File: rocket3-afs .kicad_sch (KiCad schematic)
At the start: 85 parts, among them J1 ARMING_PLUG, J2 POWER, J3 E-MATCH_DROGUE, J4 SWD, J5 E-MATCH_RECOVERY, Q1 Q_NMOS_GSD, Q2 Q_NMOS_GSD, Q3 Q_NMOS_GSD, Q4 Q_NMOS_GSD, Q5 Q_NMOS_GSD, U7 MP1584EN-LF-Z, U8 USBLC6-2SC6, U9 MMC5983MA, Y1 16MHz

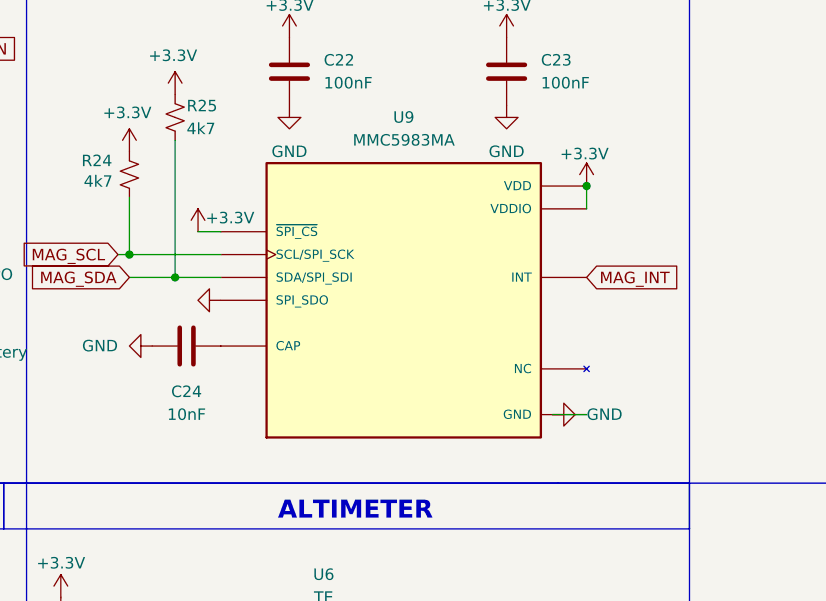
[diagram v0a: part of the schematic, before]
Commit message: Typo change on cap for magnetometer
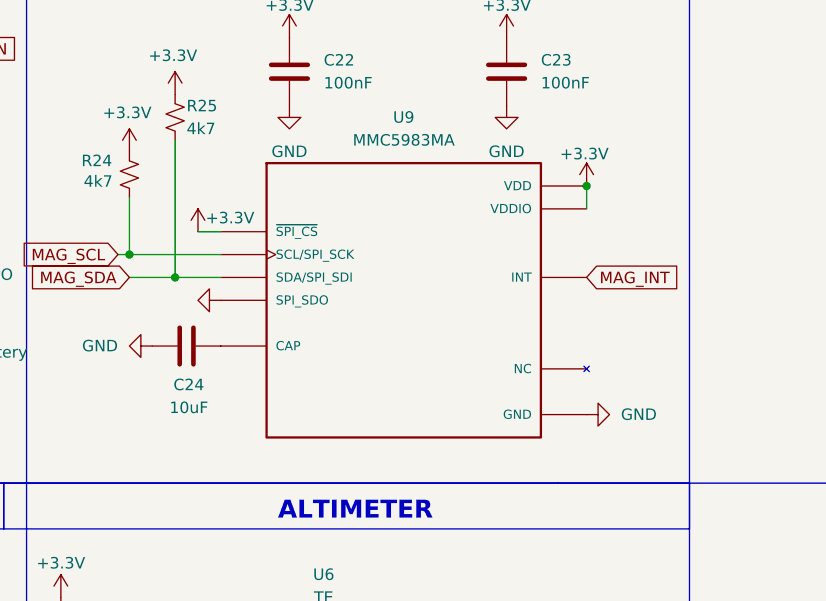
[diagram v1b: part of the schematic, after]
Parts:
- C24: value 10nF -> 10uF
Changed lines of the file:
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@@
 	(wire
 		(pts
-			(xy 287.02 123.19) (xy 283.21 123.19)
-		)
-		(stroke
-			(width 0)
-			(type default)
-		)
-	)
-	(wire
-		(pts
 			(xy 214.63 180.34) (xy 219.71 180.34)
 		)
@@
 		(on_board yes)
 		(dnp no)
-		(fields_autoplaced yes)
 		(property "Reference" "C24"
-			(at 242.57 120.65 90)
+			(at 242.824 119.888 90)
 			(effects
 				(font
@@
 			)
 		)
-		(property "Value" "10nF"
-			(at 242.57 123.19 90)
+		(property "Value" "10uF"
+			(at 242.824 122.428 90)
 			(effects
 				(font
@@
 		(lib_name "GND_3")
 		(lib_id "power:GND")
-		(at 283.21 123.19 90)
+		(at 287.02 123.19 90)
 		(unit 1)
 		(exclude_from_sim no)
@@
 		(fields_autoplaced yes)
 		(property "Reference" "#PWR095"
-			(at 289.56 123.19 0)
+			(at 293.37 123.19 0)
 			(effects
 				(font
@@
 		)
 		(property "Value" "GND"
-			(at 287.02 123.1899 90)
+			(at 290.83 123.1899 90)
 			(effects
 				(font
@@
 		)
 		(property "Footprint" ""
-			(at 283.21 123.19 0)
+			(at 287.02 123.19 0)
 			(effects
 				(font
@@
 		)
 		(property "Datasheet" ""
-			(at 283.21 123.19 0)
+			(at 287.02 123.19 0)
 			(effects
 				(font
@@
 		)
 		(property "Description" "Power symbol creates a global label with name \"GND\" , ground"
-			(at 283.21 123.19 0)
+			(at 287.02 123.19 0)
 			(effects
 				(font

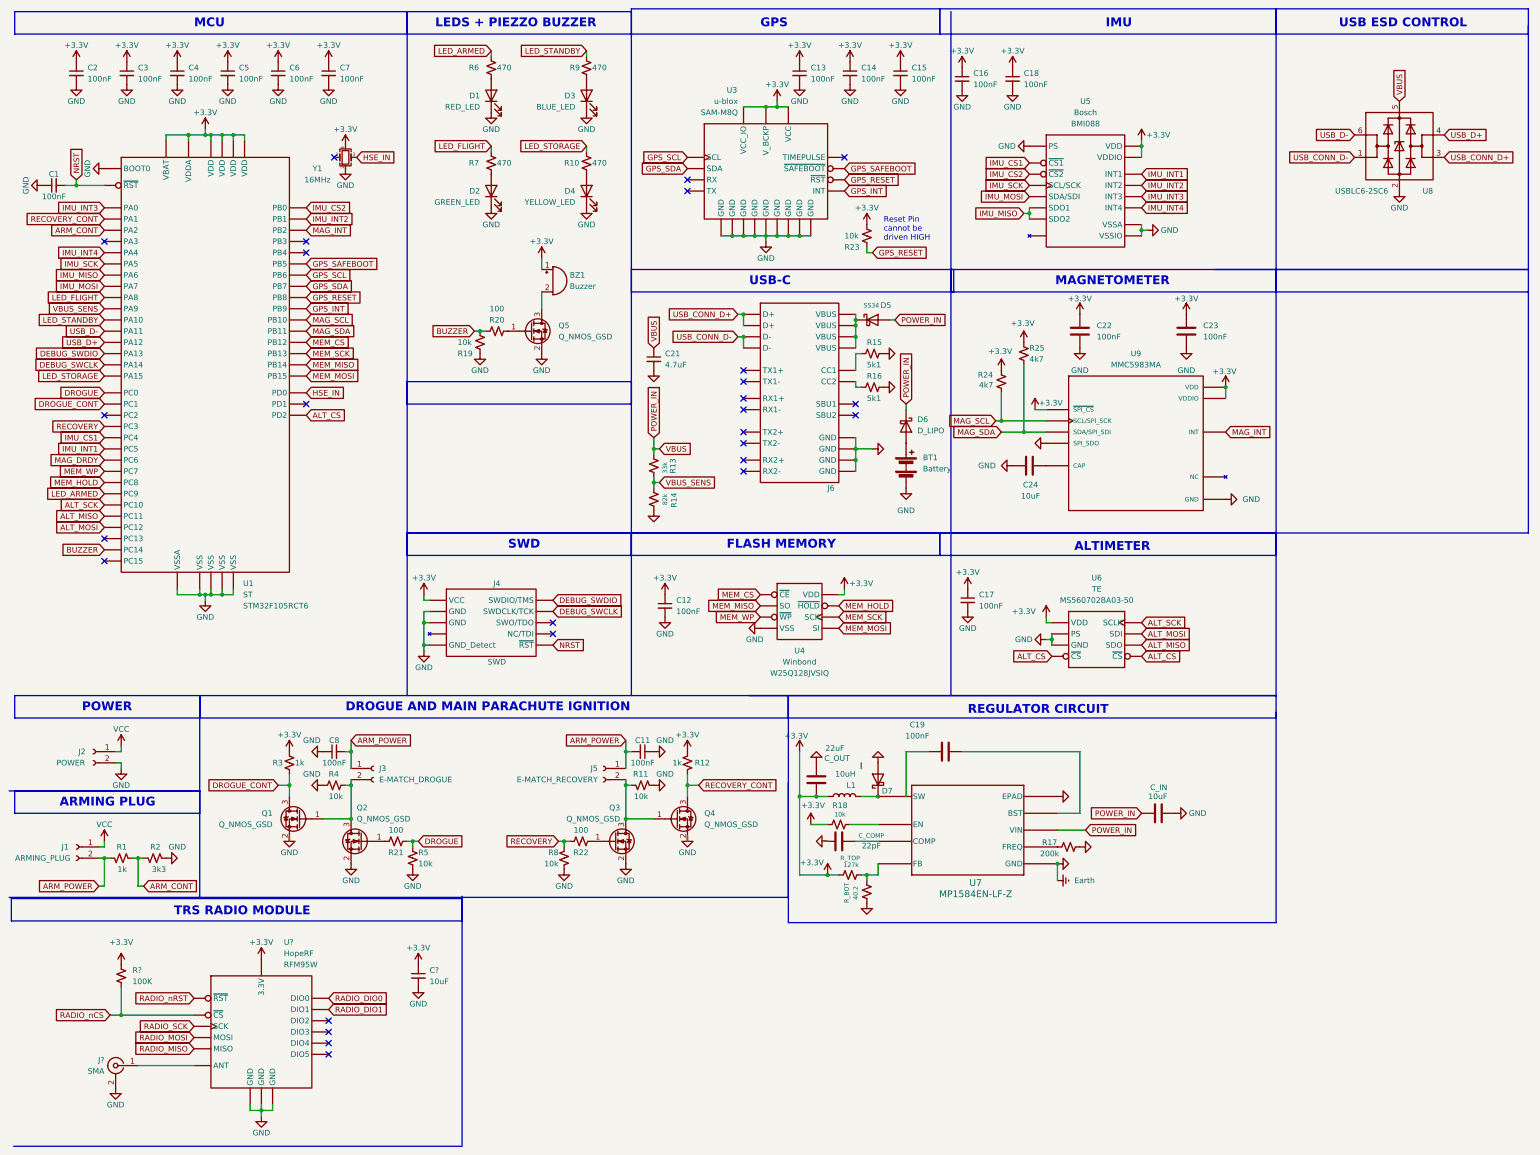
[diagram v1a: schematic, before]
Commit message: regulator circuit cleanup, added servo power and control circuits
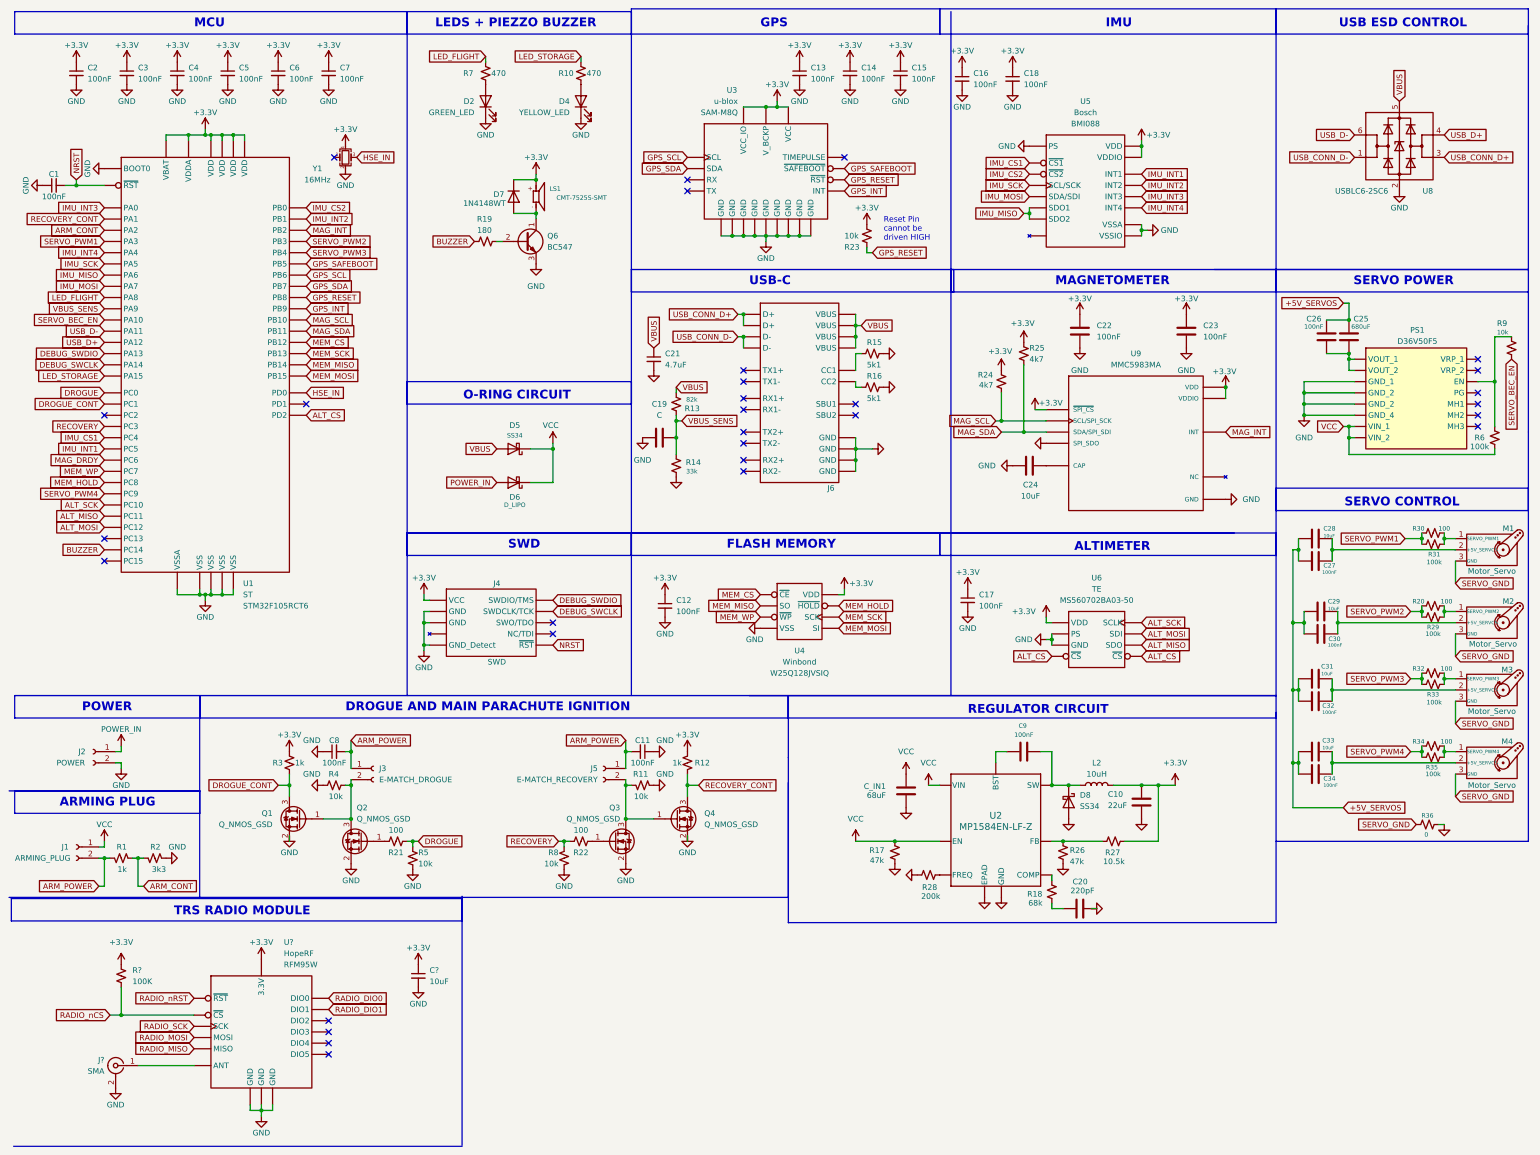
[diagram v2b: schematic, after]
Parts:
- removed BT1: Battery, symbol Device:Battery
- removed BZ1: Buzzer, Buzzer_Beeper:Buzzer_CUI_CPT-9019S-SMT, symbol Device:Buzzer
- removed C_COMP: 22pF, symbol Device:C
- removed C_IN: 10uF, symbol Device:C
- removed C_OUT: 22uF, symbol Device:C
- removed D1: RED_LED, Diode_SMD:D_0603_1608Metric, symbol Device:LED
- removed D3: BLUE_LED, Diode_SMD:D_0603_1608Metric, symbol Device:LED
- removed D7: SS34, Diode_SMD:D_SMA, symbol Diode:SS34
- removed L1: 10uH, symbol Device:L
- removed Q5: Q_NMOS_GSD, Package_TO_SOT_SMD:TSOT-23, symbol Device:Q_NMOS_GSD
- removed R_BOT: 40.2, symbol Device:R_Small_US
- removed R_TOP: 127k, symbol Device:R_Small_US
- removed U7: MP1584EN-LF-Z, SOIC8E_MPS, symbol 2025-08-17_10-37-18:MP1584EN-LF-Z
- added C10: 22uF, symbol Device:C
- added C20: 220pF, symbol Device:C
- added C25: 680uF, symbol Device:C
- added C26, C27, C30, C32, C34, C9: 100nF, symbol Device:C
- added C28, C29, C31, C33: 10uF, symbol Device:C
- added C_IN1: 68uF, symbol Device:C
- added D7: 1N4148WT, Diode_SMD:D_SOD-523, symbol Diode:1N4148WT
- added D8: SS34, Diode_SMD:D_SMA, symbol Diode:SS34
- added L2: 10uH, symbol Device:L
- added LS1: CMT-7525S-SMT, CMT-7525S-SMT:CUI_CMT-7525S-SMT, symbol CMT-7525S-SMT:CMT-7525S-SMT
- added M1, M2, M3, M4: Motor_Servo, symbol Motor:Motor_Servo
- added PS1: D36V50F5, D36V50F5, symbol D36V50F5:D36V50F5
- added Q6: BC547, Package_TO_SOT_THT:TO-92_Inline, symbol Transistor_BJT:BC547
- added R26: 47k, symbol Device:R_Small_US
- added R27: 10.5k, symbol Device:R_Small_US
- added R28: 200k, symbol Device:R_Small_US
- added R29, R31, R33, R35: 100k, symbol Device:R_Small_US
- added R30, R32, R34: 100, symbol Device:R_Small_US
- added R36: 0, symbol Device:R_Small_US
- added U2: MP1584EN-LF-Z, SOIC8E_MPS, symbol 2025-08-17_10-37-18:MP1584EN-LF-Z
- C19: value 100nF -> C
- R13: value 33k -> 82k
- R14: value 82k -> 33k
- R17: value 200k -> 47k
- R18: value 10k -> 68k
- R19: value 10k -> 180; footprint Resistor_SMD:R_0603_1608Metric -> (none); Manufacturer Generic -> (none); Part # Generic 0603 10k 1% Resistor -> (none)
- R20: footprint Resistor_SMD:R_0603_1608Metric -> (none); Manufacturer Generic -> (none); Part # Generic 0603 100 1% Resistor -> (none)
- R6: value 470 -> 100k; footprint Resistor_SMD:R_0603_1608Metric -> (none); Manufacturer Generic -> (none); Part # Generic 0603 470 1% Resistor -> (none)
- R9: value 470 -> 10k; footprint Resistor_SMD:R_0603_1608Metric -> (none); Manufacturer Generic -> (none); Part # Generic 0603 470 1% Resistor -> (none)
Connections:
- net +3.3V: now also C10.1, D7.1 (K), L2.2, LS1., R27.2; no longer R18.1
- net BUZZER: no longer R20.1
- net POWER_IN: now also D6.2 (A), J2.1 (Pin_1); no longer C21.1, D5.2 (A), D6.1 (K), R13.1, U8.5 (VBUS)
- net VBUS_SENS: now also C19.2
- net VCC: now also D5.1 (K), D6.1 (K), R17.1, R6.2, C_IN1.1, PS1. (MH3), U2. (COMP); no longer J2.1 (Pin_1)
- net at R20.2: now also M2.1 (SERVO_PWM2), R29.2
- net SERVO_BEC_EN: now reaches R9.2
- net SERVO_BEC_EN: now also U1.43 (PA10)
- net GND: now reaches C19.1
- net GND: now also C1.1, C11.1, C12.2, C13.2, C14.2, C15.2, C16.2, C17.2, C18.2, C2.2, C21.2, C22.2, C23.2, C24.1, C3.2, C4.2, C5.2, C6.2, C7.2, C8.1, C?.2, D2.1 (K), D4.1 (K), J2.2 (Pin_2), J4.3 (GND), J4.5 (GND), J4.9 (GND_Detect), J6.A1 (GND), J6.A12 (GND), J6.B1 (GND), J6.B12 (GND), J?.2 (Ext), Q1.2 (S), Q2.2 (S), Q3.2 (S), Q4.2 (S), R11.2, R14.1, R15.1, R16.1, R17.2, R2.2, R4.2, R5.2, R8.2, U1.12 (VSSA), U1.18 (VSS), U1.31 (VSS), U1.47 (VSS), U1.60 (BOOT0), U1.63 (VSS), U3.1 (GND), U3.10 (GND), U3.11 (GND), U3.15 (GND), U3.16 (GND), U3.20 (GND), U3.4 (GND), U3.5 (GND), U3.6 (GND), U4.4 (VSS), U5.4 (VSSA), U5.6 (VSSIO), U5.7 (PS), U6.2 (PS), U6.3 (GND), U8.2 (GND), U9. (GND), U?.1 (GND), U?.10 (GND), U?.8 (GND), Y1.2, C10.2, C20.2, C_IN1.2, D8.2 (A), PS1. (MH3), Q6.3 (E), R26.2, R28.2, R36.2, U2. (COMP)
- net at R18.2: now also C20.1
- net VBUS: now reaches J6.A4 (VBUS), J6.A9 (VBUS), J6.B4 (VBUS), J6.B9 (VBUS)
- net VBUS: now also C21.1, D5.2 (A), R13.1, U8.5 (VBUS); no longer D5.1 (K)
- net SERVO_PWM1: now reaches U1.17 (PA3)
- net SERVO_PWM1: now also R30.1, R31.1
- net SERVO_PWM2: now reaches U1.55 (PB3)
- net SERVO_PWM2: now also R20.1, R29.1
- net SERVO_PWM3: now reaches U1.56 (PB4)
- net SERVO_PWM3: now also R32.1, R33.1
- removed net Earth: C1.1, C11.1, C12.2, C13.2, C14.2, C15.2, C16.2, C17.2, C18.2, C2.2, C21.2, C22.2, C23.2, C24.1, C3.2, C4.2, C5.2, C6.2, C7.2, C8.1, C?.2, D2.1 (K), D4.1 (K), J2.2 (Pin_2), J4.3 (GND), J4.5 (GND), J4.9 (GND_Detect), J6.A1 (GND), J6.A12 (GND), J6.B1 (GND), J6.B12 (GND), J?.2 (Ext), Q1.2 (S), Q2.2 (S), Q3.2 (S), Q4.2 (S), R11.2, R14.1, R15.1, R16.1, R17.2, R19.2, R2.2, R4.2, R5.2, R8.2, U1.12 (VSSA), U1.18 (VSS), U1.31 (VSS), U1.47 (VSS), U1.60 (BOOT0), U1.63 (VSS), U3.1 (GND), U3.10 (GND), U3.11 (GND), U3.15 (GND), U3.16 (GND), U3.20 (GND), U3.4 (GND), U3.5 (GND), U3.6 (GND), U4.4 (VSS), U5.4 (VSSA), U5.6 (VSSIO), U5.7 (PS), U6.2 (PS), U6.3 (GND), U8.2 (GND), U9. (GND), U?.1 (GND), U?.10 (GND), U?.8 (GND), Y1.2
- net LED_ARMED: no longer names the net of R6.1
- net LED_ARMED: now also R9.1, PS1. (MH3); no longer U1.40 (PC9)
- removed net LED_STANDBY: R9.1, U1.43 (PA10)
- new net: R18.1, U2. (COMP)
- new net: R26.1, R27.1, U2. (COMP)
- new net: C9.2, D8.1 (K), L2.1, U2. (COMP)
- new net: R28.1, U2. (COMP)
- new net: C9.1, U2. (COMP)
- new net: C31.1, C32.1, M3.2 (+5V_SERVOS)
- new net: M3.1 (SERVO_PWM3), R32.2, R33.2
- new net: M1.1 (SERVO_PWM1), R30.2, R31.2
- new net: C29.1, C30.1, M2.2 (+5V_SERVOS)
- new net: C33.1, C34.1, M4.2 (+5V_SERVOS)
- new net: C25.1, C26.1, PS1. (MH3)
- new net: D7.2 (A), LS1., Q6.1 (C)
- new net: Q6.2 (B), R19.2
- new net: M4.1 (SERVO_PWM4), R34.2, R35.2
- new net: C27.1, C28.1, M1.2 (+5V_SERVOS)
- new net +5V_SERVOS: C25.2, C26.2, C27.2, C28.2, C29.2, C30.2, C31.2, C32.2, C33.2, C34.2
- new net SERVO_GND: M1.3 (GND), M2.3 (GND), M3.3 (GND), M4.3 (GND), R36.1
- new net SERVO_PWM4: R34.1, R35.1, U1.40 (PC9)
- no-connect marks 27 -> 30
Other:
- note added: "O-RING CIRCUIT"
- note added: "SERVO CONTROL"
- note added: "SERVO POWER"
- moved on the sheet: D2, D4, D5, D6, R10, R13, R14, R7
